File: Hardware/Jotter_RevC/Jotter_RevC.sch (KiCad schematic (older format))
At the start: 46 parts, among them CON1 SD_Card, P1 USB_A, P2 CONN_01X02, P3 CONN_01X02, Q1 BSS138, Q2 BSS138, SW1 SPST, U1 ATSAMD11D14A, U2 MCP73831, U3 ABS25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

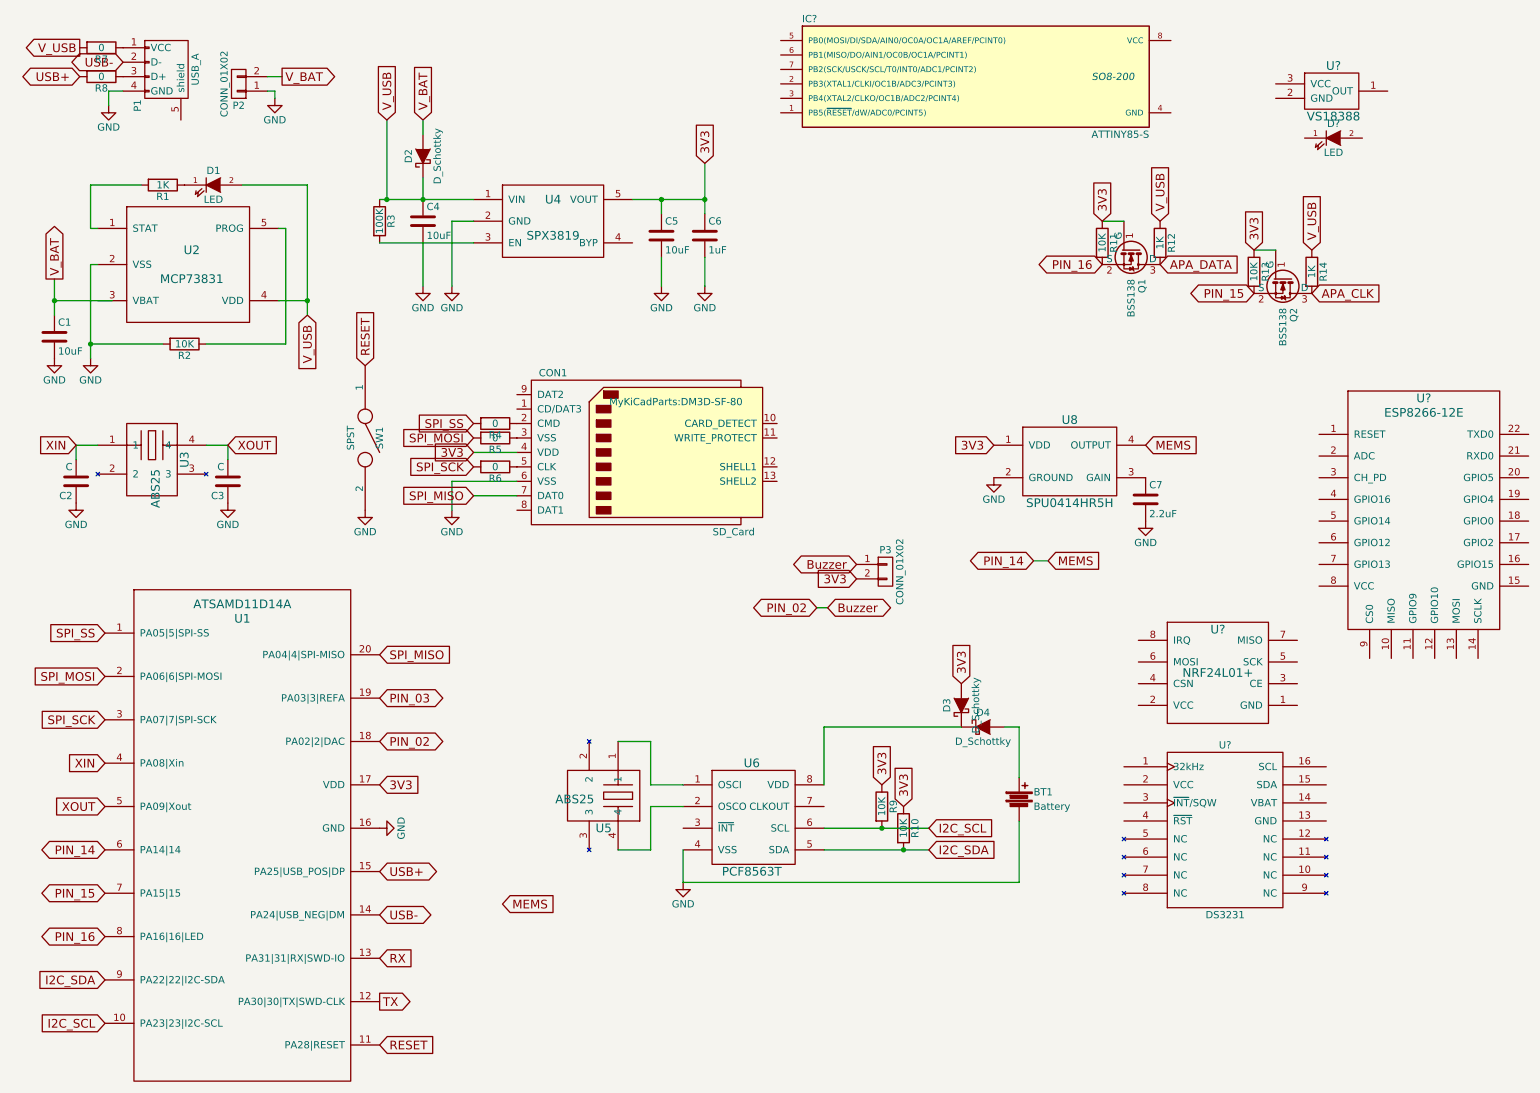
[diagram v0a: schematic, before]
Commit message: added notes on which parts to select for development; added rought shematic and layout with most selected parts on the 3in by 3in layout to get a sense of component sizes.
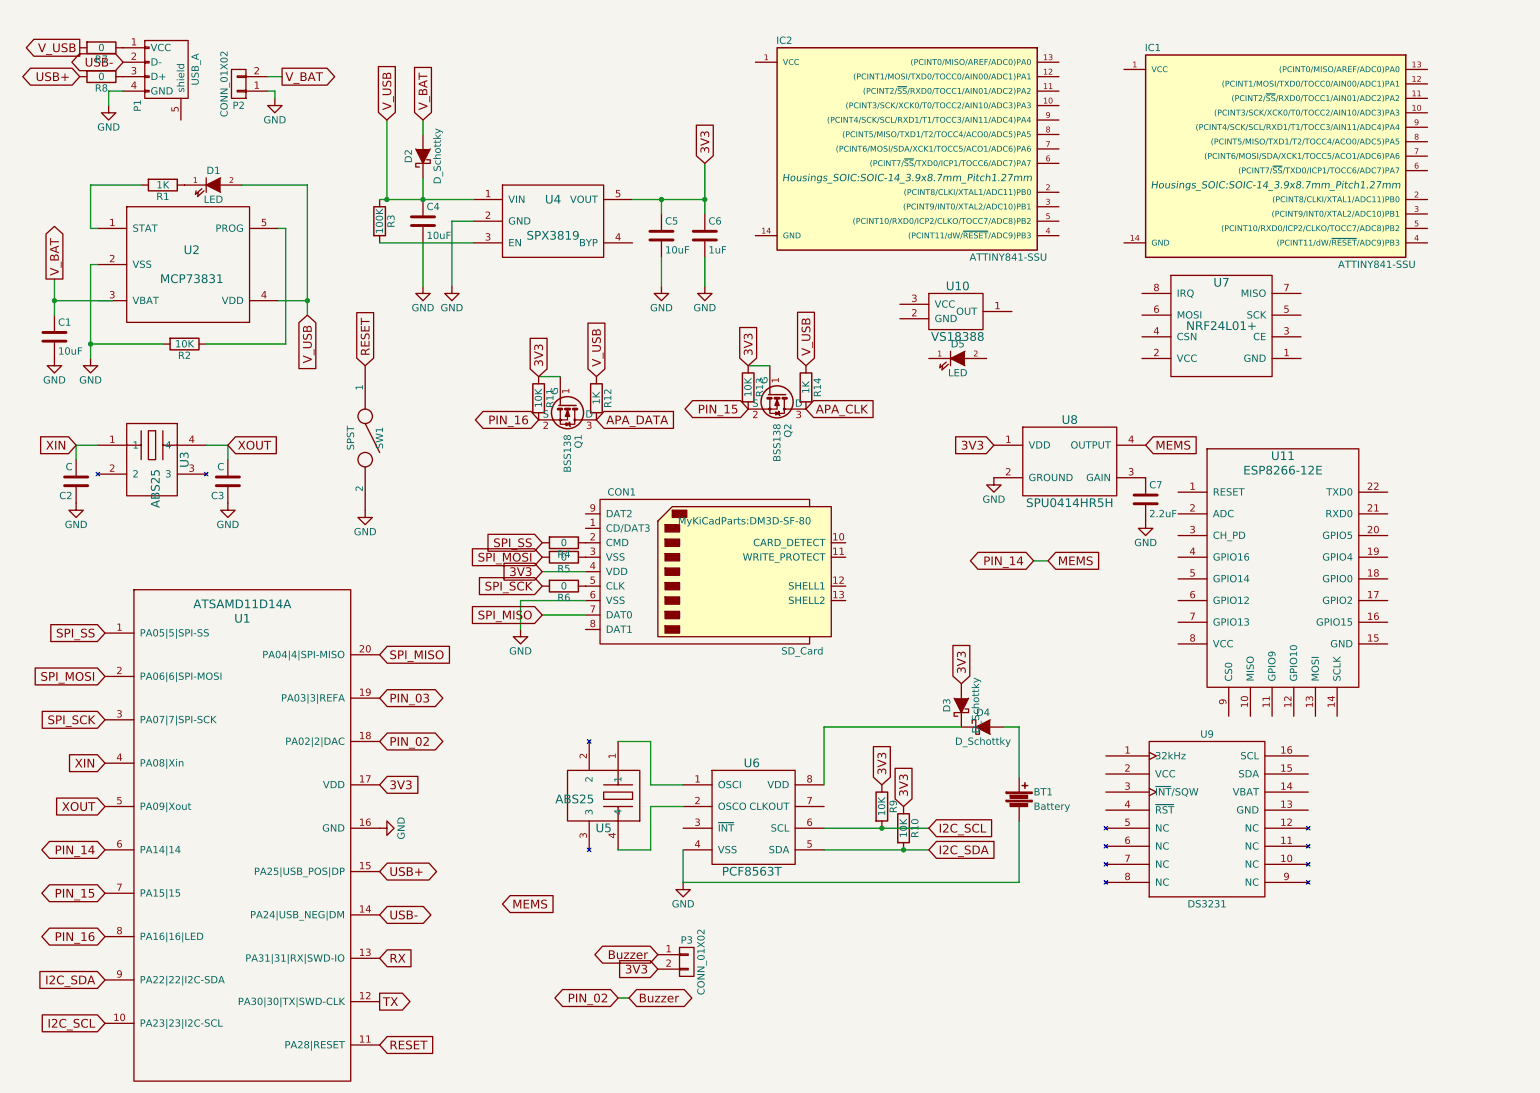
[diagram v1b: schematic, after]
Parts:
- removed IC?: ATTINY85-S, SO8-200, symbol ATTINY85-S
- added IC1, IC2: ATTINY841-SSU, Housings_SOIC:SOIC-14_3.9x8.7mm_Pitch1.27mm, symbol ATTINY841-SSU
- D5: renamed from D?; footprint (none) -> LEDs:LED-0805
- U10: renamed from U?; footprint (none) -> Pin_Headers:Pin_Header_Angled_1x03
- U11: renamed from U?; footprint (none) -> MyKiCadParts:ESP8266-12E-80
- U7: renamed from U?; footprint (none) -> MyKiCadParts:NRF24L01+
- U9: renamed from U?; footprint (none) -> MyKiCadParts:SOIC-16-W-80
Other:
- moved on the sheet: CON1, D5, P3, Q1, Q2, R11, R12, R13, R14, R4, R5, R6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
